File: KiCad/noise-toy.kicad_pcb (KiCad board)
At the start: 2 copper layers, 82.3 x 133.1 mm, 59 parts, among them J1 InputJack, J2 OutputJack, J3 Conn_02x20_PiZero, J4 Barrel_Jack_Switch, SW1 SWITCH_3PDT, SW2 SW_PUSH, SW3 SW_PUSH, SW4 SWITCH_INV, U1 MCP6002, U2 MCP3002

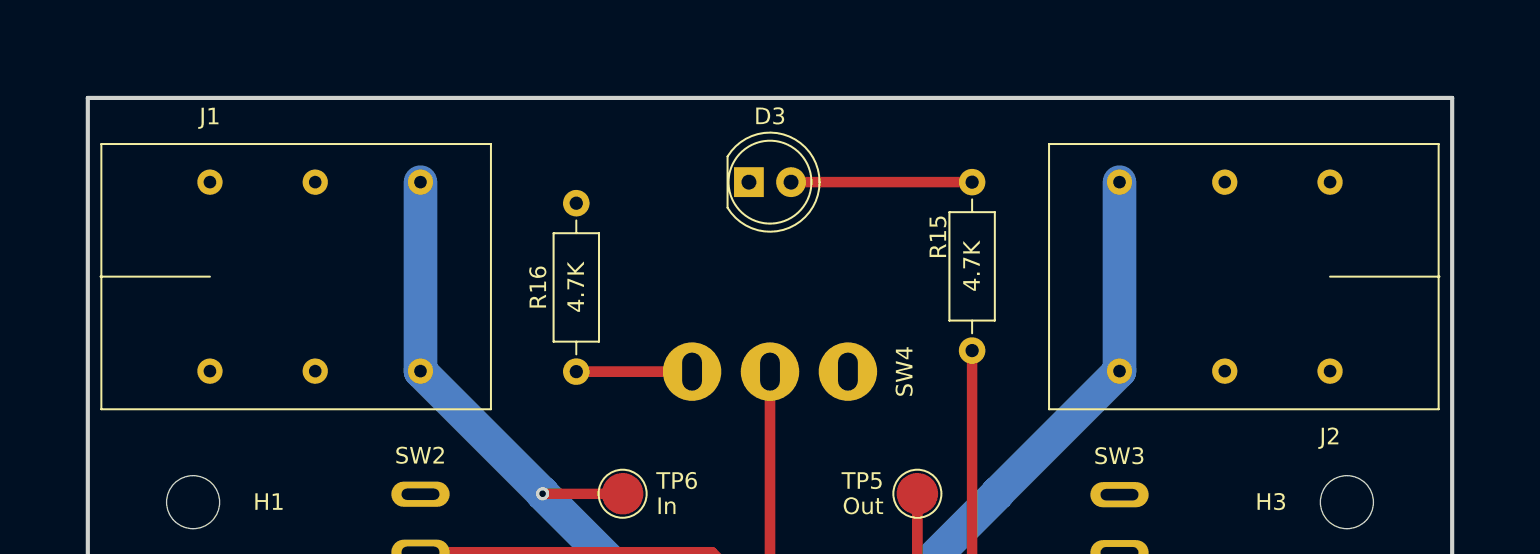
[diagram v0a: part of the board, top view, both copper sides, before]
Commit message: Fixed wrong hole size in TRS jack Moved footprints to noise-toy.pretty
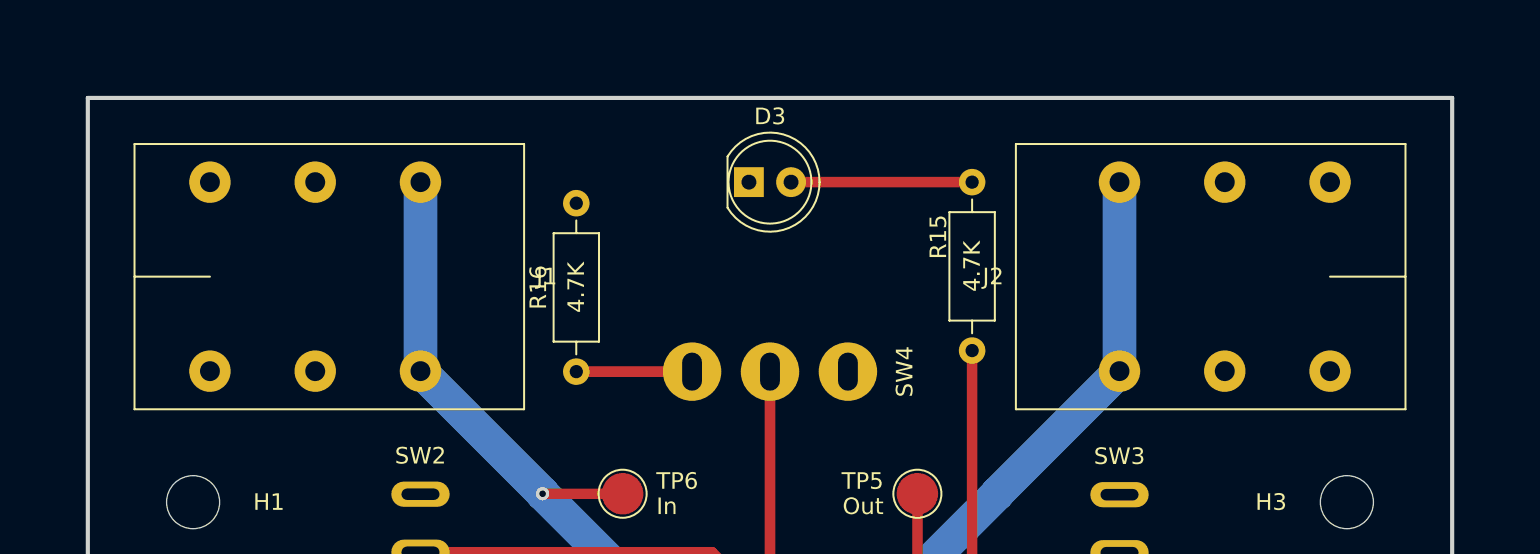
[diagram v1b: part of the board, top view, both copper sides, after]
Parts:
- J2: footprint ledlady:Audio_TRS_635_Stereo -> noise-toy:Audio_TRS_635_Stereo
- SW1: footprint ledlady:Switch_3PDT -> noise-toy:Switch_3PDT
- SW2, SW3: footprint ledlady:Button_SPST -> noise-toy:Button_SPST
- SW4: footprint ledlady:Switch_SPDT -> noise-toy:Switch_SPDT
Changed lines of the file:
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@@
     (at 101.346 42.784 180)
     (attr through_hole)
-    (fp_text reference "J1" (at 0 9.652) (layer "F.SilkS")
+    (fp_text reference "J1" (at -20.32 0) (layer "F.SilkS")
         (effects (font (size 1 1) (thickness 0.15)))
     )
@@
         (effects (font (size 1 1) (thickness 0.15)))
     )
-    (fp_line (start -16.95 -8) (end -16.95 8)
-      (stroke (width 0.12) (type solid)) (layer "F.SilkS"))
-    (fp_line (start -16.95 -8) (end 6.55 -8)
-      (stroke (width 0.12) (type solid)) (layer "F.SilkS"))
-    (fp_line (start 6.55 -8) (end 6.55 8)
-      (stroke (width 0.12) (type solid)) (layer "F.SilkS"))
-    (fp_line (start 6.55 8) (end -16.95 8)
-      (stroke (width 0.12) (type solid)) (layer "F.SilkS"))
-    (fp_line (start 6.604 0) (end 0 0)
-      (stroke (width 0.12) (type solid)) (layer "F.SilkS"))
-    (pad "1" thru_hole circle (at -12.7 -5.7 180) (size 1.524 1.524) (drill 0.762) (layers "*.Cu" "*.Mask")
+    (fp_line (start -18.95 -8) (end -18.95 8)
+      (stroke (width 0.12) (type solid)) (layer "F.SilkS"))
+    (fp_line (start -18.95 -8) (end 4.55 -8)
+      (stroke (width 0.12) (type solid)) (layer "F.SilkS"))
+    (fp_line (start 4.55 -8) (end 4.55 8)
+      (stroke (width 0.12) (type solid)) (layer "F.SilkS"))
+    (fp_line (start 4.55 0) (end 0 0)
+      (stroke (width 0.12) (type solid)) (layer "F.SilkS"))
+    (fp_line (start 4.55 8) (end -18.95 8)
+      (stroke (width 0.12) (type solid)) (layer "F.SilkS"))
+    (pad "1" thru_hole circle (at -12.7 -5.7 180) (size 2.5 2.5) (drill 1.2) (layers "*.Cu" "*.Mask")
       (net 3 "JackIn"))
-    (pad "1" thru_hole circle (at -12.7 5.7 180) (size 1.524 1.524) (drill 0.762) (layers "*.Cu" "*.Mask")
+    (pad "1" thru_hole circle (at -12.7 5.7 180) (size 2.5 2.5) (drill 1.2) (layers "*.Cu" "*.Mask")
       (net 3 "JackIn"))
-    (pad "2" thru_hole circle (at -6.35 -5.7 180) (size 1.524 1.524) (drill 0.762) (layers "*.Cu" "*.Mask")
-      (net 1 "GND"))
-    (pad "2" thru_hole circle (at -6.35 5.7 180) (size 1.524 1.524) (drill 0.762) (layers "*.Cu" "*.Mask")
-      (net 1 "GND"))
-    (pad "3" thru_hole circle (at 0 -5.7 180) (size 1.524 1.524) (drill 0.762) (layers "*.Cu" "*.Mask")
-      (net 1 "GND"))
-    (pad "3" thru_hole circle (at 0 5.7 180) (size 1.524 1.524) (drill 0.762) (layers "*.Cu" "*.Mask")
-      (net 1 "GND"))
-  )
-  (footprint "ledlady:Audio_TRS_635_Stereo" (layer "F.Cu")
+    (pad "2" thru_hole circle (at -6.35 -5.7 180) (size 2.5 2.5) (drill 1.2) (layers "*.Cu" "*.Mask")
+      (net 1 "GND"))
+    (pad "2" thru_hole circle (at -6.35 5.7 180) (size 2.5 2.5) (drill 1.2) (layers "*.Cu" "*.Mask")
+      (net 1 "GND"))
+    (pad "3" thru_hole circle (at 0 -5.7 180) (size 2.5 2.5) (drill 1.2) (layers "*.Cu" "*.Mask")
+      (net 1 "GND"))
+    (pad "3" thru_hole circle (at 0 5.7 180) (size 2.5 2.5) (drill 1.2) (layers "*.Cu" "*.Mask")
+      (net 1 "GND"))
+  )
+  (footprint "noise-toy:Audio_TRS_635_Stereo" (layer "F.Cu")
     (at 168.91 42.784)
     (attr through_hole)
-    (fp_text reference "J2" (at 0 9.652) (layer "F.SilkS")
-        (effects (font (size 1 1) (thickness 0.15)))
-    )
-    (fp_text value "OutputJack" (at 0 -9.652) (layer "F.Fab")
-        (effects (font (size 1 1) (thickness 0.15)))
-    )
-    (fp_line (start -16.95 -8) (end -16.95 8)
-      (stroke (width 0.12) (type solid)) (layer "F.SilkS"))
-    (fp_line (start -16.95 -8) (end 6.55 -8)
-      (stroke (width 0.12) (type solid)) (layer "F.SilkS"))
-    (fp_line (start 6.55 -8) (end 6.55 8)
-      (stroke (width 0.12) (type solid)) (layer "F.SilkS"))
-    (fp_line (start 6.55 8) (end -16.95 8)
-      (stroke (width 0.12) (type solid)) (layer "F.SilkS"))
-    (fp_line (start 6.604 0) (end 0 0)
-      (stroke (width 0.12) (type solid)) (layer "F.SilkS"))
-    (pad "1" thru_hole circle (at -12.7 -5.7) (size 1.524 1.524) (drill 0.762) (layers "*.Cu" "*.Mask")
+    (fp_text reference "J2" (at -20.32 0 -180) (layer "F.SilkS")
+        (effects (font (size 1 1) (thickness 0.15)))
+    )
+    (fp_text value "OutputJack" (at 0 -9.652 -180) (layer "F.Fab")
+        (effects (font (size 1 1) (thickness 0.15)))
+    )
+    (fp_line (start -18.95 -8) (end -18.95 8)
+      (stroke (width 0.12) (type solid)) (layer "F.SilkS"))
+    (fp_line (start -18.95 -8) (end 4.55 -8)
+      (stroke (width 0.12) (type solid)) (layer "F.SilkS"))
+    (fp_line (start 4.55 -8) (end 4.55 8)
+      (stroke (width 0.12) (type solid)) (layer "F.SilkS"))
+    (fp_line (start 4.55 0) (end 0 0)
+      (stroke (width 0.12) (type solid)) (layer "F.SilkS"))
+    (fp_line (start 4.55 8) (end -18.95 8)
+      (stroke (width 0.12) (type solid)) (layer "F.SilkS"))
+    (pad "1" thru_hole circle (at -12.7 -5.7) (size 2.5 2.5) (drill 1.2) (layers "*.Cu" "*.Mask")
       (net 4 "JackOut"))
-    (pad "1" thru_hole circle (at -12.7 5.7) (size 1.524 1.524) (drill 0.762) (layers "*.Cu" "*.Mask")
+    (pad "1" thru_hole circle (at -12.7 5.7) (size 2.5 2.5) (drill 1.2) (layers "*.Cu" "*.Mask")
       (net 4 "JackOut"))
-    (pad "2" thru_hole circle (at -6.35 -5.7) (size 1.524 1.524) (drill 0.762) (layers "*.Cu" "*.Mask")
-      (net 1 "GND"))
-    (pad "2" thru_hole circle (at -6.35 5.7) (size 1.524 1.524) (drill 0.762) (layers "*.Cu" "*.Mask")
-      (net 1 "GND"))
-    (pad "3" thru_hole circle (at 0 -5.7) (size 1.524 1.524) (drill 0.762) (layers "*.Cu" "*.Mask")
-      (net 1 "GND"))
-    (pad "3" thru_hole circle (at 0 5.7) (size 1.524 1.524) (drill 0.762) (layers "*.Cu" "*.Mask")
+    (pad "2" thru_hole circle (at -6.35 -5.7) (size 2.5 2.5) (drill 1.2) (layers "*.Cu" "*.Mask")
+      (net 1 "GND"))
+    (pad "2" thru_hole circle (at -6.35 5.7) (size 2.5 2.5) (drill 1.2) (layers "*.Cu" "*.Mask")
+      (net 1 "GND"))
+    (pad "3" thru_hole circle (at 0 -5.7) (size 2.5 2.5) (drill 1.2) (layers "*.Cu" "*.Mask")
+      (net 1 "GND"))
+    (pad "3" thru_hole circle (at 0 5.7) (size 2.5 2.5) (drill 1.2) (layers "*.Cu" "*.Mask")
       (net 1 "GND"))
   )
@@
       (net 43 "Net-(C5-Pad2)"))
   )
-  (footprint "ledlady:Switch_3PDT" (layer "F.Cu")
+  (footprint "noise-toy:Switch_3PDT" (layer "F.Cu")
     (at 135.128 77.978 180)
     (attr through_hole)
@@
       (net 53 "/Bypass"))
   )
-  (footprint "ledlady:Button_SPST" (layer "F.Cu")
+  (footprint "noise-toy:Button_SPST" (layer "F.Cu")
     (at 114.046 57.658 180)
     (attr through_hole)
@@
       (net 1 "GND"))
   )
-  (footprint "ledlady:Button_SPST" (layer "F.Cu")
+  (footprint "noise-toy:Button_SPST" (layer "F.Cu")
     (at 156.21 57.686 180)
     (attr through_hole)
@@
       (net 1 "GND"))
   )
-  (footprint "ledlady:Switch_SPDT" (layer "F.Cu")
+  (footprint "noise-toy:Switch_SPDT" (layer "F.Cu")
     (at 135.128 48.514 90)
     (attr through_hole)

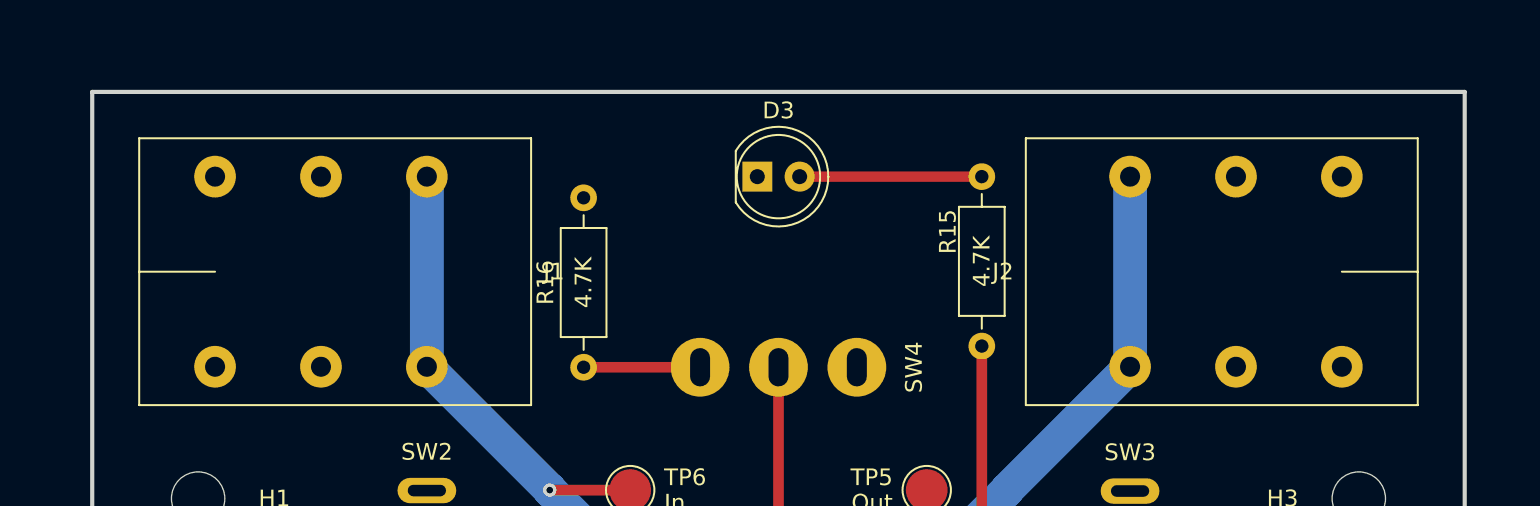
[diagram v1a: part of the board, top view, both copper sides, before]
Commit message: Changed position of TRS jack
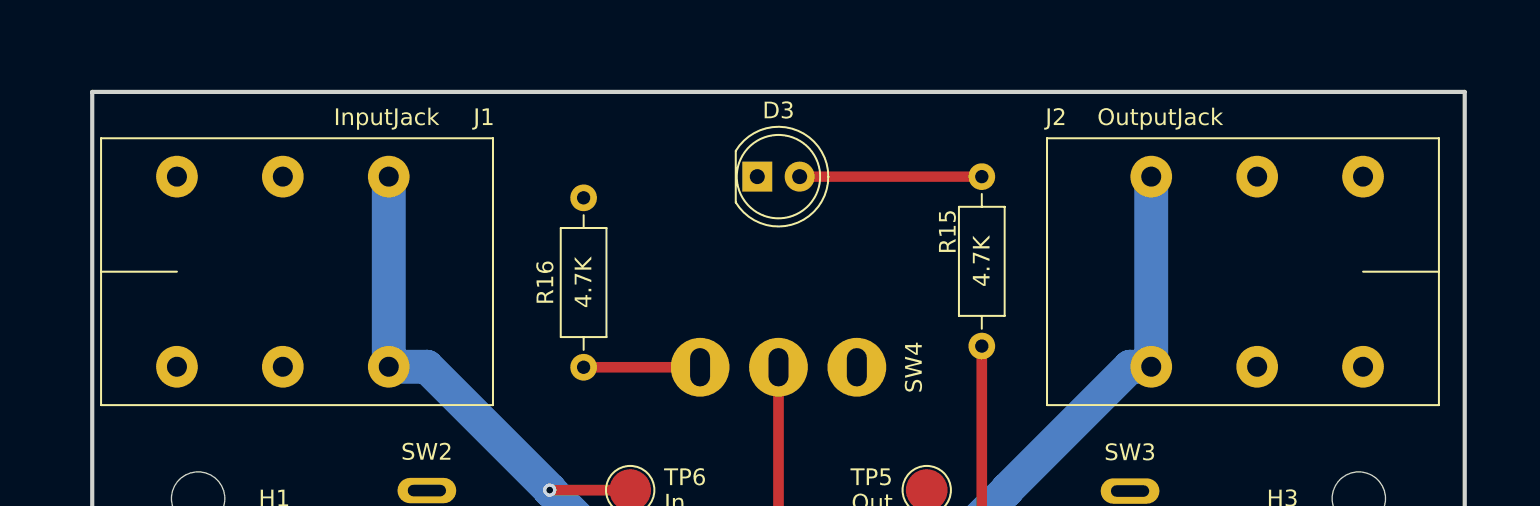
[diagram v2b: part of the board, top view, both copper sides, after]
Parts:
- moved J1 2.29 mm to (99.1, 42.8)
- moved J2 1.27 mm to (170.2, 42.8)
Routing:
- net JackIn: track 53.7 -> 56.0 mm
- net JackOut: track 53.7 -> 55.0 mm
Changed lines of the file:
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@@
   )
   (footprint "ledlady:Audio_TRS_635_Stereo" (layer "F.Cu")
-    (at 101.346 42.784 180)
+    (at 99.06 42.784 180)
     (attr through_hole)
-    (fp_text reference "J1" (at -20.32 0) (layer "F.SilkS")
-        (effects (font (size 1 1) (thickness 0.15)))
+    (fp_text reference "J1" (at -19.05 9.256) (layer "F.SilkS")
+        (effects (font (size 1 1) (thickness 0.15)) (justify right))
     )
-    (fp_text value "InputJack" (at 0 -9.652) (layer "F.Fab")
-        (effects (font (size 1 1) (thickness 0.15)))
+    (fp_text value "InputJack" (at -9.398 9.256) (layer "F.SilkS")
+        (effects (font (size 1 1) (thickness 0.15)) (justify left))
     )
     (fp_line (start -18.95 -8) (end -18.95 8)
@@
   )
   (footprint "noise-toy:Audio_TRS_635_Stereo" (layer "F.Cu")
-    (at 168.91 42.784)
+    (at 170.18 42.784)
     (attr through_hole)
-    (fp_text reference "J2" (at -20.32 0 -180) (layer "F.SilkS")
-        (effects (font (size 1 1) (thickness 0.15)))
+    (fp_text reference "J2" (at -19.05 -9.256 180) (layer "F.SilkS")
+        (effects (font (size 1 1) (thickness 0.15)) (justify left))
     )
-    (fp_text value "OutputJack" (at 0 -9.652 -180) (layer "F.Fab")
-        (effects (font (size 1 1) (thickness 0.15)))
+    (fp_text value "OutputJack" (at -8.382 -9.256 180) (layer "F.SilkS")
+        (effects (font (size 1 1) (thickness 0.15)) (justify right))
     )
     (fp_line (start -18.95 -8) (end -18.95 8)
@@
   (segment (start 126.238 55.88) (end 121.412 55.88) (width 0.635) (layer "F.Cu") (net 3))
   (via (at 121.412 55.88) (size 0.8) (drill 0.4) (layers "F.Cu" "B.Cu") (net 3))
+  (segment (start 111.76 48.484) (end 111.76 37.084) (width 2.032) (layer "B.Cu") (net 3))
   (segment (start 126.238 76.879844) (end 126.238 60.706) (width 2.032) (layer "B.Cu") (net 3))
   (segment (start 114.046 48.484) (end 121.412 55.85) (width 2.032) (layer "B.Cu") (net 3))
@@
   (segment (start 129.828 77.978) (end 127.336156 77.978) (width 2.032) (layer "B.Cu") (net 3))
   (segment (start 121.412 55.88) (end 126.238 60.706) (width 2.032) (layer "B.Cu") (net 3))
-  (segment (start 114.046 37.084) (end 114.046 48.484) (width 2.032) (layer "B.Cu") (net 3))
+  (segment (start 114.046 48.484) (end 111.76 48.484) (width 2.032) (layer "B.Cu") (net 3))
   (segment (start 144.018 60.706) (end 144.018 60.706) (width 0.635) (layer "F.Cu") (net 4))
   (segment (start 144.018 55.88) (end 144.018 60.706) (width 0.635) (layer "F.Cu") (net 4))
   (via (at 144.018 60.706) (size 0.8) (drill 0.4) (layers "F.Cu" "B.Cu") (net 4))
+  (segment (start 156.21 48.484) (end 157.48 48.484) (width 2.032) (layer "B.Cu") (net 4))
   (segment (start 148.844 55.85) (end 148.844 55.88) (width 2.032) (layer "B.Cu") (net 4))
   (segment (start 148.844 55.88) (end 144.018 60.706) (width 2.032) (layer "B.Cu") (net 4))
   (segment (start 156.21 48.484) (end 148.844 55.85) (width 2.032) (layer "B.Cu") (net 4))
-  (segment (start 156.21 37.084) (end 156.21 48.484) (width 2.032) (layer "B.Cu") (net 4))
   (segment (start 142.919844 77.978) (end 144.018 76.879844) (width 2.032) (layer "B.Cu") (net 4))
   (segment (start 144.018 76.879844) (end 144.018 60.706) (width 2.032) (layer "B.Cu") (net 4))
   (segment (start 140.428 77.978) (end 142.919844 77.978) (width 2.032) (layer "B.Cu") (net 4))
+  (segment (start 157.48 48.484) (end 157.48 37.084) (width 2.032) (layer "B.Cu") (net 4))
   (segment (start 106.934 86.614) (end 106.934 86.614) (width 0.635) (layer "F.Cu") (net 5))
   (segment (start 164.084 108.204) (end 164.084 114.554) (width 0.635) (layer "F.Cu") (net 5))

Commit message: Added attribution to pcb
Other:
- board text added: "Ce sera comme si je t'avais donné, au lieu d'étoiles, des tas de petits grelots qui savent rire... Noise-Toy Rev.0 CC-BY electrosmash.com Ledlady 2023"
- board text removed: "Ce sera comme si je t'avais donné, au lieu d'étoiles, des tas de petits grelots qui savent rire... Noise-Toy Rev.0 Ledlady 2023"
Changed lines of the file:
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@@
       (drillshape 0)
       (scaleselection 1)
-      (outputdirectory "gerber/")
+      (outputdirectory "../Production/GerberFiles/")
     )
   )
@@
   (gr_line (start 93.98 32.004) (end 176.276 32.004)
     (stroke (width 0.25) (type solid)) (layer "Edge.Cuts"))
-  (gr_text "Ce sera comme si je t'avais donné,\nau lieu d'étoiles, des tas de petits grelots\nqui savent rire... \n\nNoise-Toy Rev.0\nLedlady 2023" (at 125.476 150.495) (layer "F.SilkS")
+  (gr_text "Ce sera comme si je t'avais donné,\nau lieu d'étoiles, des tas de petits grelots\nqui savent rire... \n\nNoise-Toy Rev.0\nCC-BY electrosmash.com\nLedlady 2023" (at 125.476 150.495) (layer "F.SilkS")
     (effects (font (size 1 1) (thickness 0.2)) (justify left))
   )
